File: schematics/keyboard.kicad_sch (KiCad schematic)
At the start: 33 parts, among them J3 Mini-DIN-6, Q1 2N7000, Q3 2N7000, Q4 2N7000, Q5 2N7000, U1 74HC595, U13 ATF22V10C-7, U14 74HC14, U15 74HC280, U18 74HC04, U19 74HC00, U4 74HC595, U5 74HC165, U6 74HC165

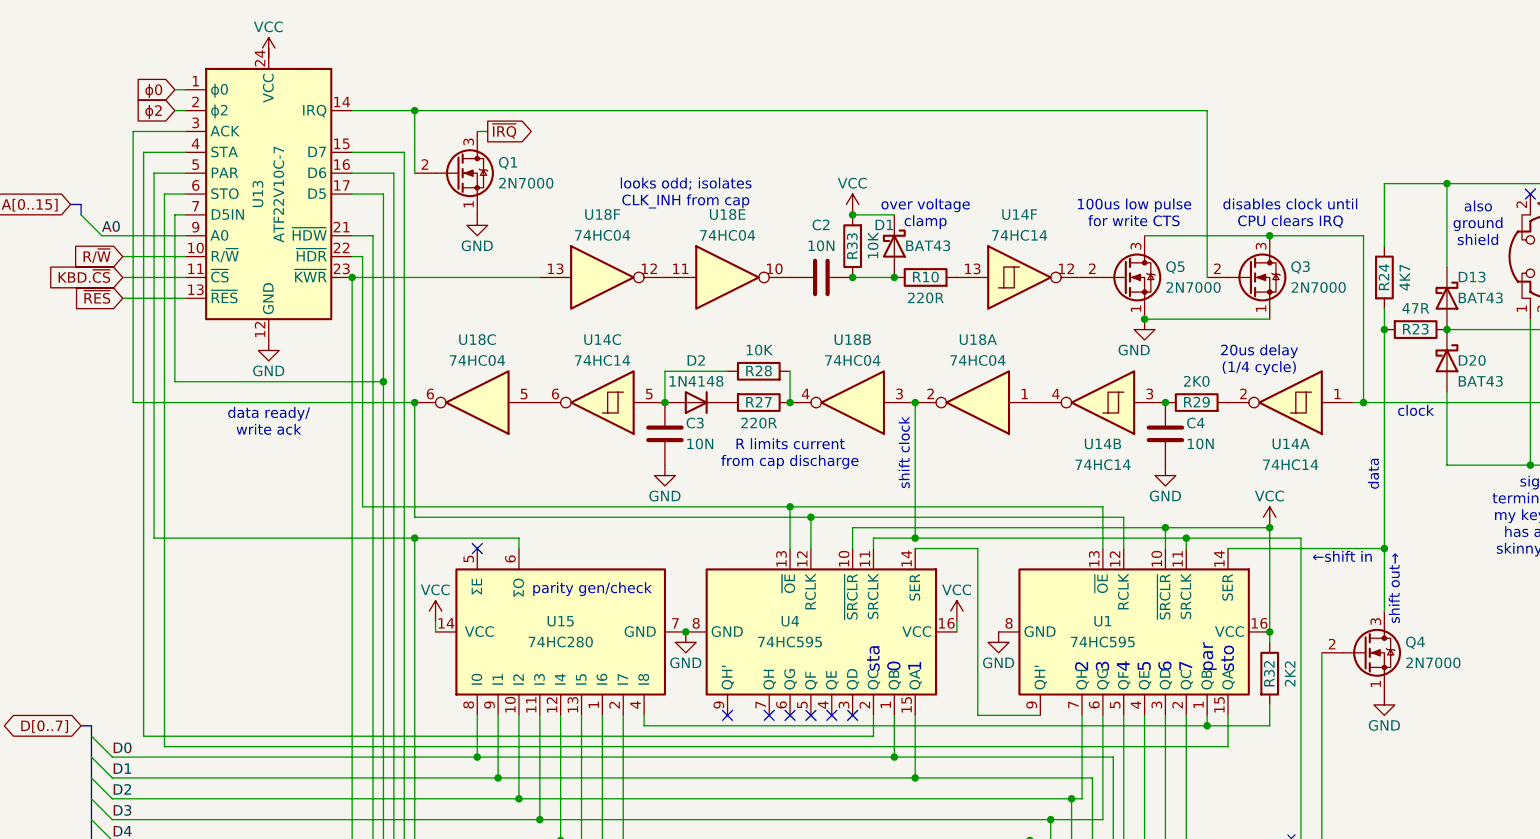
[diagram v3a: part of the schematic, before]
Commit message: fixes to bootloader; finished via schematic
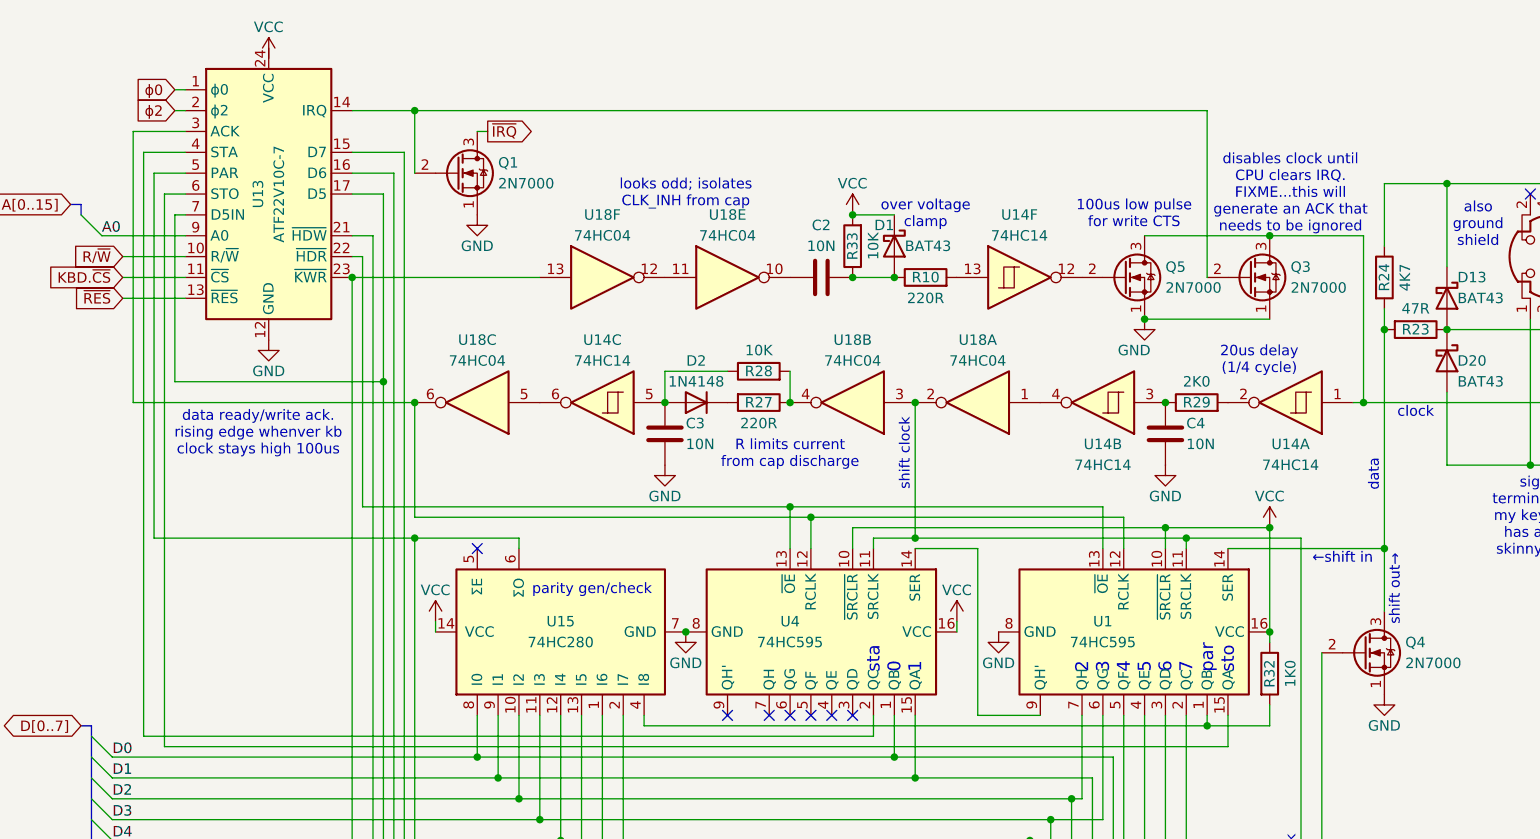
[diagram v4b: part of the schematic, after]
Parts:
- R32: value 2K2 -> 1K0
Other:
- note added: "data ready/write ack. rising edge whenver kb clock stays high 100us"
- note added: "disables clock until CPU clears IRQ. FIXME...this will generate an ACK that needs to be ignored"
- note removed: "data ready/ write ack"
- note removed: "disables clock until CPU clears IRQ"
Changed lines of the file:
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@@
 		)
 	)
-	(text "data ready/\nwrite ack"
+	(text "data ready/write ack.\nrising edge whenver kb\nclock stays high 100us"
 		(exclude_from_sim no)
-		(at 69.85 72.39 0)
+		(at 68.58 73.66 0)
 		(effects
 			(font
@@
 		)
 	)
-	(text "disables clock until\nCPU clears IRQ"
+	(text "disables clock until\nCPU clears IRQ.\nFIXME...this will\ngenerate an ACK that\nneeds to be ignored"
 		(exclude_from_sim no)
-		(at 194.31 46.99 0)
+		(at 194.31 44.45 0)
 		(effects
 			(font
@@
 			)
 		)
-		(property "Value" "2K2"
+		(property "Value" "1K0"
 			(at 194.31 102.87 90)
 			(show_name no)

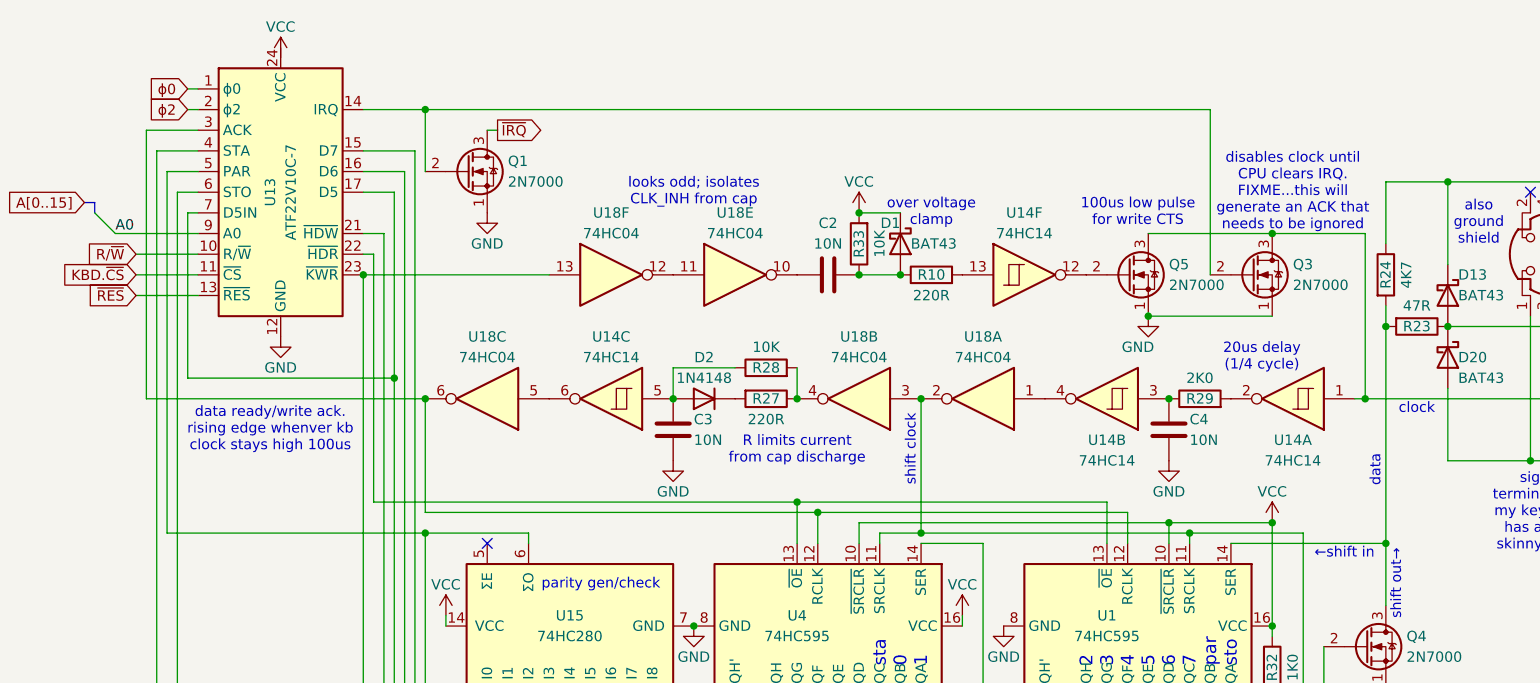
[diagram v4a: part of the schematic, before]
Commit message: fix keyboard irq clear
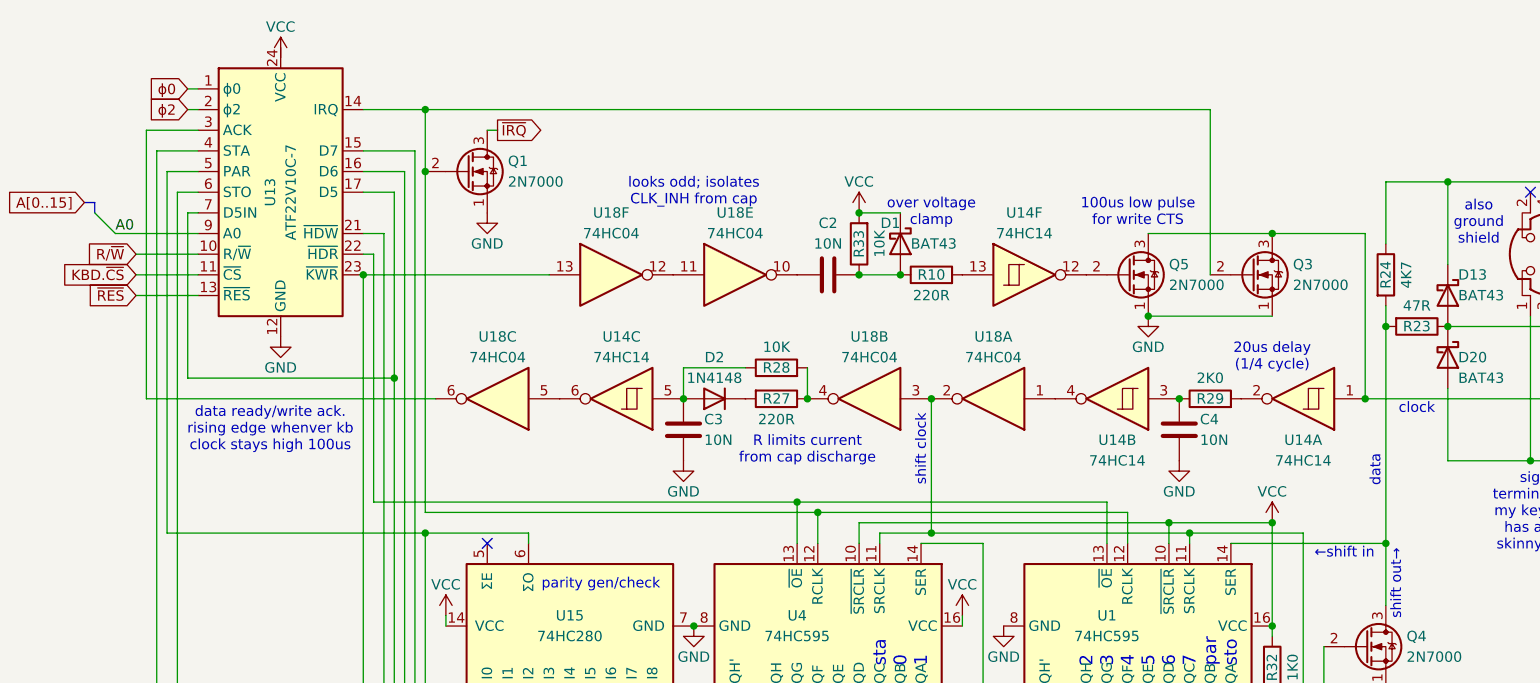
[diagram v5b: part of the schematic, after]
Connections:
- net at U1.12 (RCLK), U4.12 (RCLK): now also Q1.2 (G), Q3.2 (G), U13.14 (IRQ); no longer U13.3 (ACK), U18.6
- new net: U13.3 (ACK), U18.6
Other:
- note removed: "disables clock until CPU clears IRQ. FIXME...this will generate an ACK that needs to be ignored"
- moved on the sheet: C3, C4, D2, R27, R28, R29, U14A, U14B, U14C, U18A, U18B, U18C

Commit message: updating schematics as I wire the board
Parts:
- renumbered C3 to C13, C2 to C14, C4 to C15, D2 to D10, D1 to D11, D13 to D12, D20 to D13, D9 to D14, D10 to D15, J3 to J2, Q5 to Q2, R28 to R33, R27 to R34, R33 to R35, R10 to R36, R29 to R37, R32 to R38, R24 to R39, R23 to R40, R3 to R41, R16 to R42, U14 to U18, U18 to U19, U19 to U20, U13 to U21, U15 to U22, U5 to U23, U4 to U24, U6 to U25, U1 to U26

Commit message: updating schematics as I wire the board
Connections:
- net GND: now also U19.13; no longer U19.9
- net VCC: now also U21.24 (VCC)
- net at U19.3, U23.2 (CLK), U24.11 (SRCLK)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: now also U19.6; no longer U19.2
- net at Q2.2 (G): now also U18.8; no longer U18.12
- net at Q2.3 (D), Q3.3 (D), R41.2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: now also U18.5; no longer U18.1
- net at R36.2: now also U18.9; no longer U18.13
- net at U21.23 (~{KWR}), U23.15 (CLK_INH), U25.15 (CLK_INH): now also U19.11; no longer U19.13
- net at U21.3 (ACK): now also U19.2; no longer U19.6
- net at R37.2: now also U18.6; no longer U18.2
- net at C13.1, D10.2 (A), R33.1: now also U18.1; no longer U18.5
- net at U18.4: now also U19.5; no longer U19.1
- net at C14.1: now also U19.8; no longer U19.10
- new net: U18.2, U19.1
- new net: U19.10, U19.9
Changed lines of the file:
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@@
 		(lib_id "74xx:74HC04")
 		(at 49.53 190.5 90)
-		(unit 4)
+		(unit 6)
 		(body_style 1)
 		(exclude_from_sim no)
@@
 				(path "/94c72abe-aaa5-49aa-8ab7-5d3e7cbc10be/a706df21-fd6c-437e-86a1-96397867f2ab"
 					(reference "U19")
-					(unit 4)
+					(unit 6)
 				)
 			)
@@
 		(lib_id "74xx:74HC14")
 		(at 195.58 69.85 180)
-		(unit 1)
+		(unit 3)
 		(body_style 1)
 		(exclude_from_sim no)
@@
 				(path "/94c72abe-aaa5-49aa-8ab7-5d3e7cbc10be/a706df21-fd6c-437e-86a1-96397867f2ab"
 					(reference "U18")
-					(unit 1)
+					(unit 3)
 				)
 			)
@@
 		(lib_id "74xx:74HC04")
 		(at 157.48 69.85 180)
-		(unit 1)
+		(unit 3)
 		(body_style 1)
 		(exclude_from_sim no)
@@
 				(path "/94c72abe-aaa5-49aa-8ab7-5d3e7cbc10be/a706df21-fd6c-437e-86a1-96397867f2ab"
 					(reference "U19")
-					(unit 1)
+					(unit 3)
 				)
 			)
@@
 		(lib_id "74xx:74HC04")
 		(at 96.52 69.85 180)
-		(unit 3)
+		(unit 1)
 		(body_style 1)
 		(exclude_from_sim no)
@@
 				(path "/94c72abe-aaa5-49aa-8ab7-5d3e7cbc10be/a706df21-fd6c-437e-86a1-96397867f2ab"
 					(reference "U19")
-					(unit 3)
+					(unit 1)
 				)
 			)
@@
 	(symbol
 		(lib_id "power:VCC")
-		(at 69.85 27.94 0)
+		(at 69.85 26.67 0)
 		(unit 1)
 		(body_style 1)
@@
 		(dnp no)
 		(property "Reference" "#PWR047"
-			(at 69.85 31.75 0)
+			(at 69.85 30.48 0)
 			(hide yes)
 			(show_name no)
@@
 		)
 		(property "Value" "VCC"
-			(at 69.85 24.13 0)
+			(at 69.85 22.86 0)
 			(show_name no)
 			(do_not_autoplace no)
@@
 		)
 		(property "Footprint" ""
-			(at 69.85 27.94 0)
+			(at 69.85 26.67 0)
 			(hide yes)
 			(show_name no)
@@
 		)
 		(property "Datasheet" ""
-			(at 69.85 27.94 0)
+			(at 69.85 26.67 0)
 			(hide yes)
 			(show_name no)
@@
 		)
 		(property "Description" "Power symbol creates a global label with name \"VCC\""
-			(at 69.85 27.94 0)
+			(at 69.85 26.67 0)
 			(hide yes)
 			(show_name no)
@@
 		(lib_id "74xx:74HC14")
 		(at 161.29 54.61 0)
-		(unit 6)
+		(unit 4)
 		(body_style 1)
 		(exclude_from_sim no)
@@
 				(path "/94c72abe-aaa5-49aa-8ab7-5d3e7cbc10be/a706df21-fd6c-437e-86a1-96397867f2ab"
 					(reference "U18")
-					(unit 6)
+					(unit 4)
 				)
 			)
@@
 		(lib_id "74xx:74HC04")
 		(at 110.49 54.61 0)
-		(unit 6)
+		(unit 5)
 		(body_style 1)
 		(exclude_from_sim no)
@@
 				(path "/94c72abe-aaa5-49aa-8ab7-5d3e7cbc10be/a706df21-fd6c-437e-86a1-96397867f2ab"
 					(reference "U19")
-					(unit 6)
+					(unit 5)
 				)
 			)
@@
 		(lib_id "74xx:74HC04")
 		(at 125.73 54.61 0)
-		(unit 5)
+		(unit 4)
 		(body_style 1)
 		(exclude_from_sim no)
@@
 				(path "/94c72abe-aaa5-49aa-8ab7-5d3e7cbc10be/a706df21-fd6c-437e-86a1-96397867f2ab"
 					(reference "U19")
-					(unit 5)
+					(unit 4)
 				)
 			)
@@
 		(lib_id "74xx:74HC14")
 		(at 111.76 69.85 180)
-		(unit 3)
+		(unit 1)
 		(body_style 1)
 		(exclude_from_sim no)
@@
 				(path "/94c72abe-aaa5-49aa-8ab7-5d3e7cbc10be/a706df21-fd6c-437e-86a1-96397867f2ab"
 					(reference "U18")
-					(unit 3)
+					(unit 1)
 				)
 			)

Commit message: fixing wiring
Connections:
- net D5: now also U21.8 (D5IN); no longer U21.7 (D5IN)
- net at U24.2 (QC): now also U21.5 (STA); no longer U21.4 (STA)
- net at U21.3: no longer U19.2
- net at U22.6 (ΣO), U23.4 (F): now also U21.6 (PAR); no longer U21.5 (PAR)
- net at U26.15 (QA): now also U21.7 (STO); no longer U21.6 (STO)
- new net: U19.2, U21.4 (ACK)
